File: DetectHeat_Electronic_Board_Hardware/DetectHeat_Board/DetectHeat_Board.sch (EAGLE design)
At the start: 24 parts, among them SW1 430182043816, SW2 450302014072, T1 *BC847, U1 PIC18F14K22-I/SS

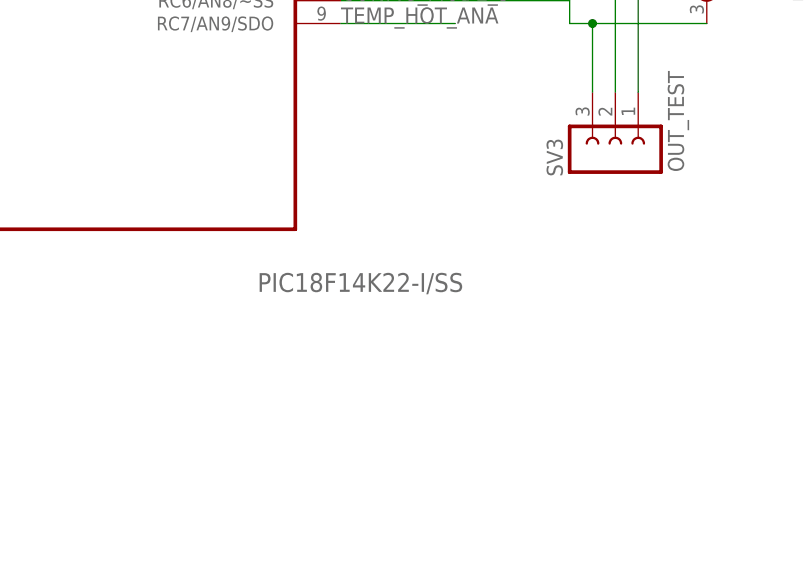
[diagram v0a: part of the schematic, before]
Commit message: correct little mistake : PIC reference
PIC18F14K22 --> PIC18LF14K22 (low energy)
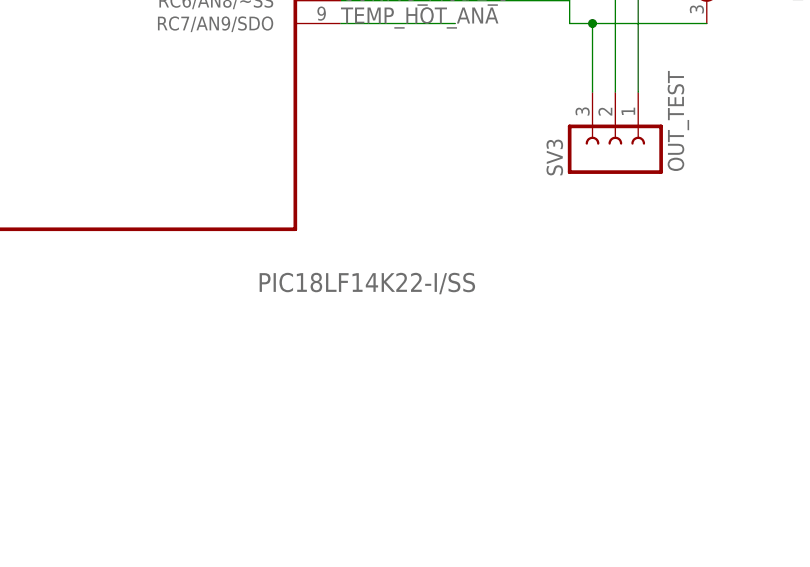
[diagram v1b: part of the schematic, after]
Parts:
- U1: value PIC18F14K22-I/SS -> PIC18LF14K22-I/SS; device Composants_Actif_Lib:PIC18F14K22-I/SS -> Composants_Actif_Lib:PIC18LF14K22-I/SS
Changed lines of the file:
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@@
 <part name="TEMP_COLD" library="Composants_Actif_Lib" deviceset="MCP9700A-E/TO" device=""/>
 <part name="TEMP_HOT" library="Composants_Actif_Lib" deviceset="MCP9700A-E/TO" device=""/>
-<part name="U1" library="Composants_Actif_Lib" deviceset="PIC18F14K22-I/SS" device=""/>
+<part name="U1" library="Composants_Actif_Lib" deviceset="PIC18LF14K22-I/SS" device=""/>
 <part name="SG3" library="buzzer" deviceset="F/EE17P" device=""/>
 <part name="BATTERY_CR2032" library="Composants_Connectiques_Lib" deviceset="BATTERY_1236_C" device=""/>
